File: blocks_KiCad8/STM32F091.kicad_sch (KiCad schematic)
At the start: 11 parts

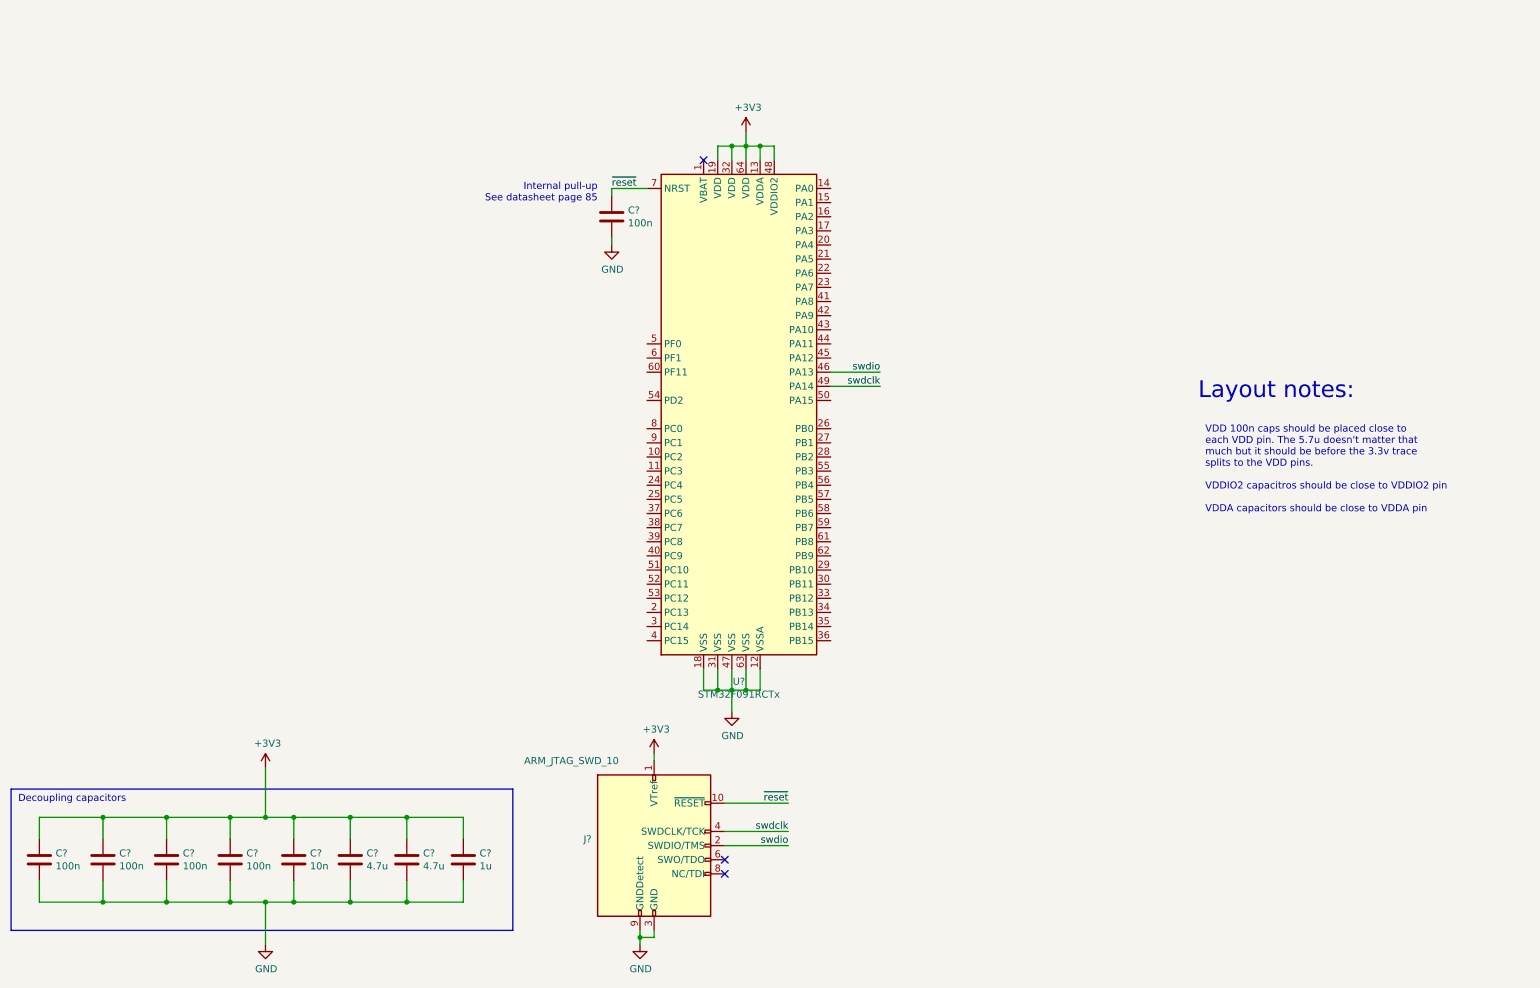
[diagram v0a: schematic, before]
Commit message: changed standard blocks, minor changes to some footprints
Adjusted solder mask expansion on debug connector
Added TPS7A LDO footrpint and symbol
Added crystal to MCU standard block.
Added status lights to MCU standard block.
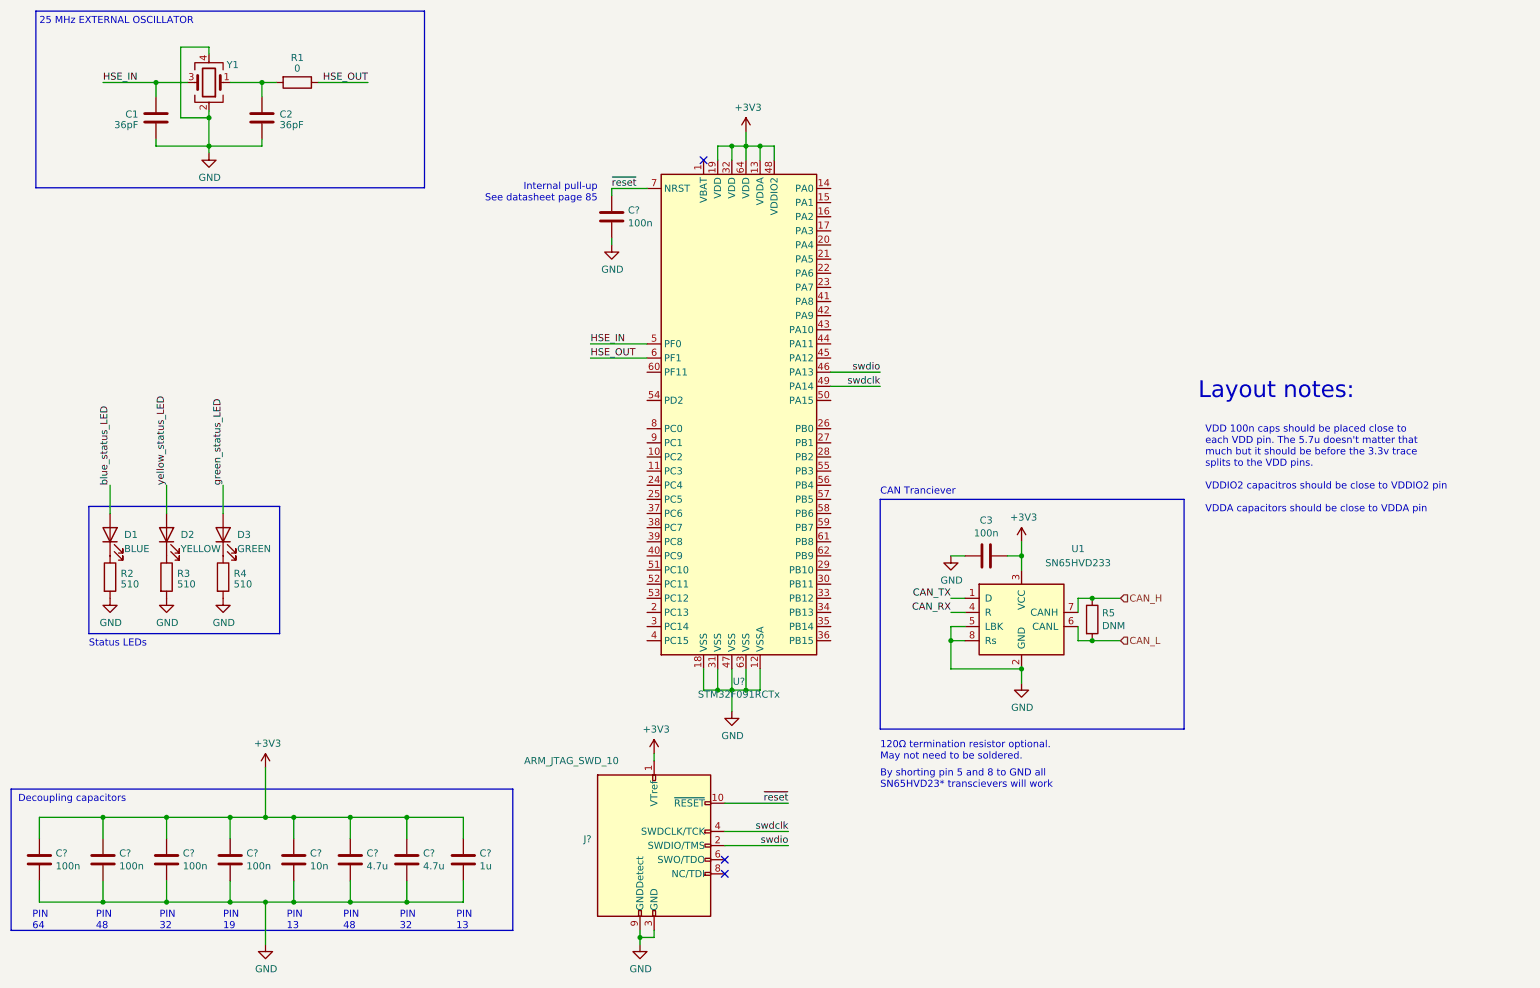
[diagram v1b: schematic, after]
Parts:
- added C1, C2: 36pF, Capacitor_SMD:C_0603_1608Metric_Pad1.08x0.95mm_HandSolder, symbol Device:C
- added C3: 100n, Capacitor_SMD:C_0603_1608Metric, symbol Device:C
- added D1: BLUE, LED_SMD:LED_0603_1608Metric, symbol Device:LED
- added D2: YELLOW, LED_SMD:LED_0603_1608Metric, symbol Device:LED
- added D3: GREEN, LED_SMD:LED_0603_1608Metric, symbol Device:LED
- added R1: 0, Resistor_SMD:R_0603_1608Metric_Pad0.98x0.95mm_HandSolder, symbol Device:R
- added R2, R3, R4: 510, Resistor_SMD:R_0603_1608Metric, symbol Device:R
- added R5: DNM, Resistor_SMD:R_0603_1608Metric, symbol Device:R
- added U1: SN65HVD233, Package_SO:SOIC-8_3.9x4.9mm_P1.27mm, symbol Interface_CAN_LIN:SN65HVD233
- added Y1: Crystal_GND24, Crystal:Crystal_SMD_3225-4Pin_3.2x2.5mm_HandSoldering, symbol Device:Crystal_GND24
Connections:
- net +3V3: now also C3.1, U1.3 (VCC)
- net GND: now also C1.2, C2.2, C3.2, R2.2, R3.2, R4.2, U1.2 (GND), U1.5 (LBK), U1.8 (Rs), Y1.2, Y1.4
- net HSE_IN: now reaches U?.5 (PF0)
- net HSE_IN: now also C1.1, Y1.3
- net HSE_OUT: now reaches U?.6 (PF1)
- net HSE_OUT: now also R1.1
- new net: D1.1 (K), R2.1
- new net: D3.1 (K), R4.1
- new net: C2.1, R1.2, Y1.1
- new net: D2.1 (K), R3.1
- new net CAN_H: R5.1, U1.7 (CANH)
- new net CAN_L: R5.2, U1.6 (CANL)
- new net CAN_RX: U1.4 (R)
- new net CAN_TX: U1.1 (D)
- new net blue_status_LED: D1.2 (A)
- new net green_status_LED: D3.2 (A)
- new net yellow_status_LED: D2.2 (A)
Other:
- note added: "120Ω termination resistor optional. May not need to be soldered."
- note added: "25 MHz EXTERNAL OSCILLATOR"
- note added: "By shorting pin 5 and 8 to GND all SN65HVD23* transcievers will work"
- note added: "CAN Tranciever"
- note added: "PIN 13"
- note added: "PIN 19"
- note added: "PIN 32"
- note added: "PIN 48"
- note added: "PIN 64"
- note added: "Status LEDs"
